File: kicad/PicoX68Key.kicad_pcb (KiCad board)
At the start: 2 copper layers, 33.9 x 69 mm, 22 parts, among them J1 LED_BOARD, J2 MINI-DIN-7, Q1 2N7000, Q2 2N7000, Q3 2N7000, U1 Pico

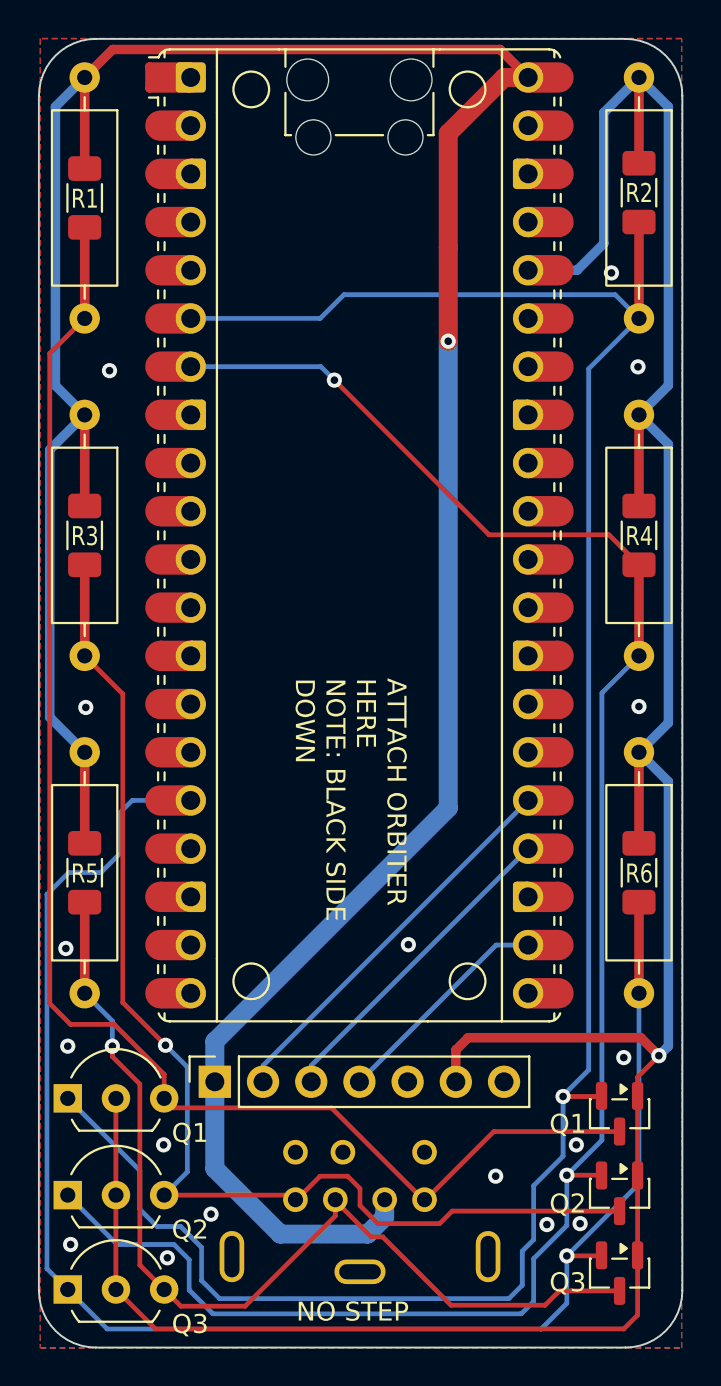
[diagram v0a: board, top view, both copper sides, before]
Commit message: Add LED sub-board
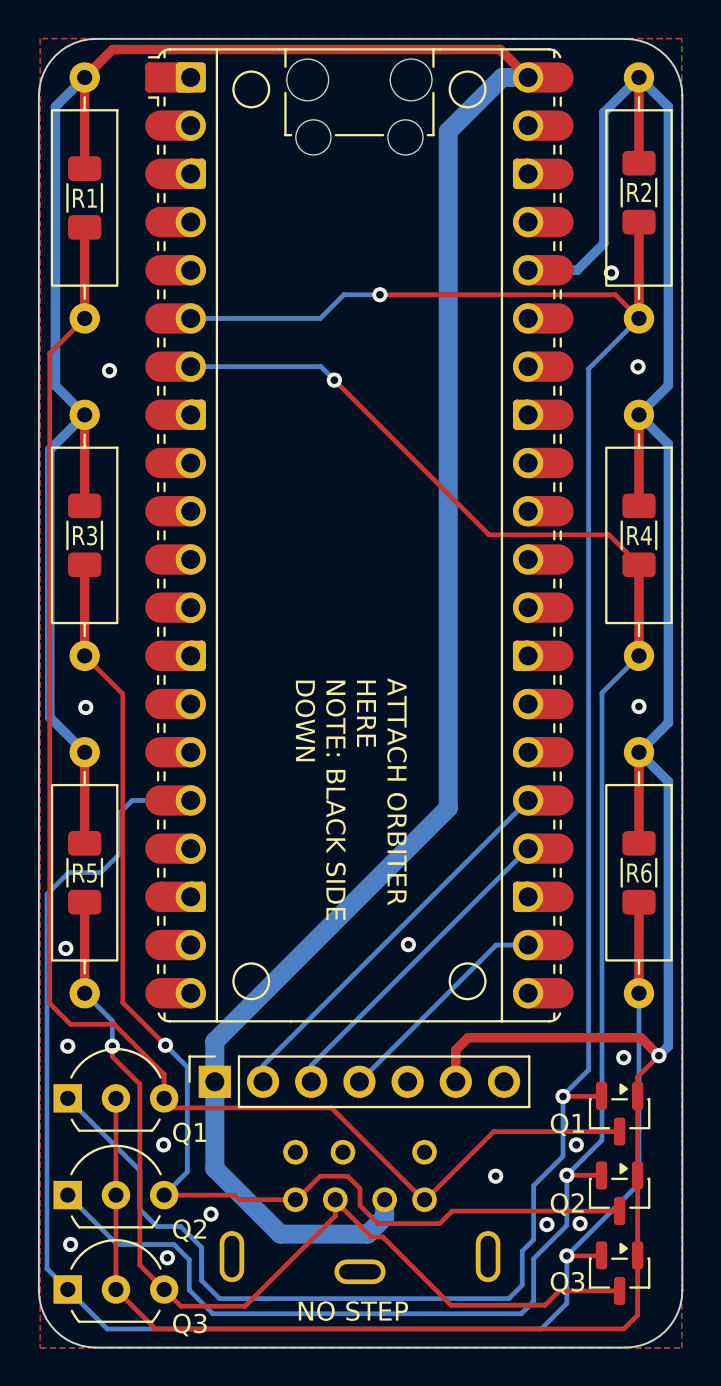
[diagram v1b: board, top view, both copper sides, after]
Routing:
- net VBUS: track 154.0 -> 154.1 mm, vias 1 -> 0
- net KB_TX_L: vias 1 -> 2
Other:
- board text added: "Designed by RetroSwim Thanks to Zuofo, Guddler, tmk"
- board text added: "https://github.com/retroswim/PicoX68Key"
- board text added: "日本のアミーガ"
- board text removed: "@retroswim@bitbang.social twitch.tv/retroswim"
- board text removed: "Designed by RetroSwim"
- board text removed: "https://github.com/retroswimau/PicoX68Key"
